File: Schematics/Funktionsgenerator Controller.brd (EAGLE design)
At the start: 58 x 51.3 mm, 35 parts, among them IC1 ATMEGA328PB-AU, IC2 TLE4270-2D, IC3 AD9833BRMZ, IC4 LM318D, IC5 LM318D, X1 22-23-2051, X3 22-23-2031, X4 22-23-2031, X5 22-23-2031, X6 22-23-2031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

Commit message: Added Resistor to limit current for TFT Backlight
Das TFT Display wurde zu heiß, da der Vorwiderstand für die Hintergrundbeleuchtung des TFT lediglich 6Ohm beträgt. Durch einen weiteren Vorwiderstand von 22Ohm konnte die Wärmeentwicklung des Displays erheblich reduziert werden ohne eine merkliche Reduzierung der Helligkeit. Alternativ wäre zu überlegen ob ein Trimmer zur Justierung eingebaut werden sollte
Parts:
- removed C3: EEEFT1V470AR, SamacSys_Parts:EEEFT(C)
- added C15: TAJD476K010R, SamacSys_Parts:CAPPM7344X310N
- added R7: 22, resistor:R0603
- C1, C11, C12, C13, C14, C7, C8: value 100nF -> 100n
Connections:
- new net N$18: P1.LED+, R7.1
- net GND: now also C15.2; no longer C3.2
- net VCC: now also C15.1, R7.2; no longer C3.1, P1.LED+
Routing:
- net VCC: track 178.8 -> 173.3 mm
- net N$18: track 0.00 -> 2.96 mm
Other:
- board text removed: "C:/Users/dem40095/Downloads/404px-sam_and_max_sth.bmp"
- board text removed: "C:/Users/dem40095/Downloads/flat,800x800,075,f.u5.bmp"

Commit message: VCC on encoder connector for external pull-up
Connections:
- net GND: no longer X1.4
- net VCC: now also X1.4
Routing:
- net VCC: track 173.3 -> 186.4 mm
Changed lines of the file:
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@@
 <layer number="14" name="Route14" color="1" fill="6" visible="no" active="no"/>
 <layer number="15" name="Route15" color="4" fill="6" visible="no" active="no"/>
-<layer number="16" name="Bottom" color="1" fill="1" visible="yes" active="yes"/>
+<layer number="16" name="Bottom" color="1" fill="1" visible="no" active="yes"/>
 <layer number="17" name="Pads" color="2" fill="1" visible="yes" active="yes"/>
 <layer number="18" name="Vias" color="2" fill="1" visible="yes" active="yes"/>
@@
 <layer number="20" name="Dimension" color="24" fill="1" visible="yes" active="yes"/>
 <layer number="21" name="tPlace" color="7" fill="1" visible="yes" active="yes"/>
-<layer number="22" name="bPlace" color="7" fill="1" visible="yes" active="yes"/>
+<layer number="22" name="bPlace" color="7" fill="1" visible="no" active="yes"/>
 <layer number="23" name="tOrigins" color="15" fill="1" visible="yes" active="yes"/>
-<layer number="24" name="bOrigins" color="15" fill="1" visible="yes" active="yes"/>
+<layer number="24" name="bOrigins" color="15" fill="1" visible="no" active="yes"/>
 <layer number="25" name="tNames" color="7" fill="1" visible="yes" active="yes"/>
-<layer number="26" name="bNames" color="7" fill="1" visible="yes" active="yes"/>
+<layer number="26" name="bNames" color="7" fill="1" visible="no" active="yes"/>
 <layer number="27" name="tValues" color="7" fill="1" visible="no" active="yes"/>
 <layer number="28" name="bValues" color="7" fill="1" visible="no" active="yes"/>
@@
 <layer number="38" name="bTest" color="7" fill="1" visible="no" active="yes"/>
 <layer number="39" name="tKeepout" color="4" fill="11" visible="yes" active="yes"/>
-<layer number="40" name="bKeepout" color="1" fill="11" visible="yes" active="yes"/>
+<layer number="40" name="bKeepout" color="1" fill="11" visible="no" active="yes"/>
 <layer number="41" name="tRestrict" color="4" fill="10" visible="yes" active="yes"/>
-<layer number="42" name="bRestrict" color="1" fill="10" visible="yes" active="yes"/>
+<layer number="42" name="bRestrict" color="1" fill="10" visible="no" active="yes"/>
 <layer number="43" name="vRestrict" color="2" fill="10" visible="no" active="yes"/>
 <layer number="44" name="Drills" color="7" fill="1" visible="no" active="yes"/>
@@
 <layer number="49" name="Reference" color="7" fill="1" visible="no" active="yes"/>
 <layer number="50" name="dxf" color="7" fill="1" visible="no" active="no"/>
-<layer number="51" name="tDocu" color="7" fill="1" visible="yes" active="yes"/>
-<layer number="52" name="bDocu" color="7" fill="1" visible="yes" active="yes"/>
+<layer number="51" name="tDocu" color="7" fill="1" visible="no" active="yes"/>
+<layer number="52" name="bDocu" color="7" fill="1" visible="no" active="yes"/>
 <layer number="53" name="tGND_GNDA" color="7" fill="9" visible="no" active="no"/>
 <layer number="54" name="bGND_GNDA" color="1" fill="9" visible="no" active="no"/>
@@
 <wire x1="40.64" y1="41.91" x2="40.64" y2="43.6" width="0.3048" layer="16"/>
 <wire x1="40.64" y1="43.6" x2="39.37" y2="44.87" width="0.3048" layer="16"/>
+<contactref element="X1" pad="4"/>
+<wire x1="45.5422" y1="34.4297" x2="46.3169" y2="33.655" width="0.3048" layer="1"/>
+<wire x1="46.3169" y1="33.655" x2="52.07" y2="33.655" width="0.3048" layer="1"/>
+<wire x1="52.07" y1="33.655" x2="52.705" y2="34.29" width="0.3048" layer="1"/>
+<wire x1="50.8" y1="38.1" x2="50.038" y2="38.1" width="0.3048" layer="1"/>
+<wire x1="52.705" y1="34.29" x2="52.705" y2="36.195" width="0.3048" layer="1"/>
+<wire x1="52.705" y1="36.195" x2="50.8" y2="38.1" width="0.3048" layer="1"/>
 </signal>
 <signal name="GND">
@@
 <via x="43.4975" y="12.3825" extent="1-16" drill="0.85"/>
 <via x="20.32" y="37.7825" extent="1-16" drill="0.85"/>
-<contactref element="X1" pad="2"/>
-<contactref element="X1" pad="4"/>
 <wire x1="23.055" y1="37.0775" x2="21.025" y2="37.0775" width="0.3048" layer="1"/>
 <wire x1="21.025" y1="37.0775" x2="20.32" y2="37.7825" width="0.3048" layer="1"/>
@@
 <wire x1="36.1125" y1="36.2775" x2="36.195" y2="36.195" width="0.3048" layer="1"/>
 <contactref element="C15" pad="2"/>
+<contactref element="X1" pad="2"/>
 </signal>
 <signal name="+12V">

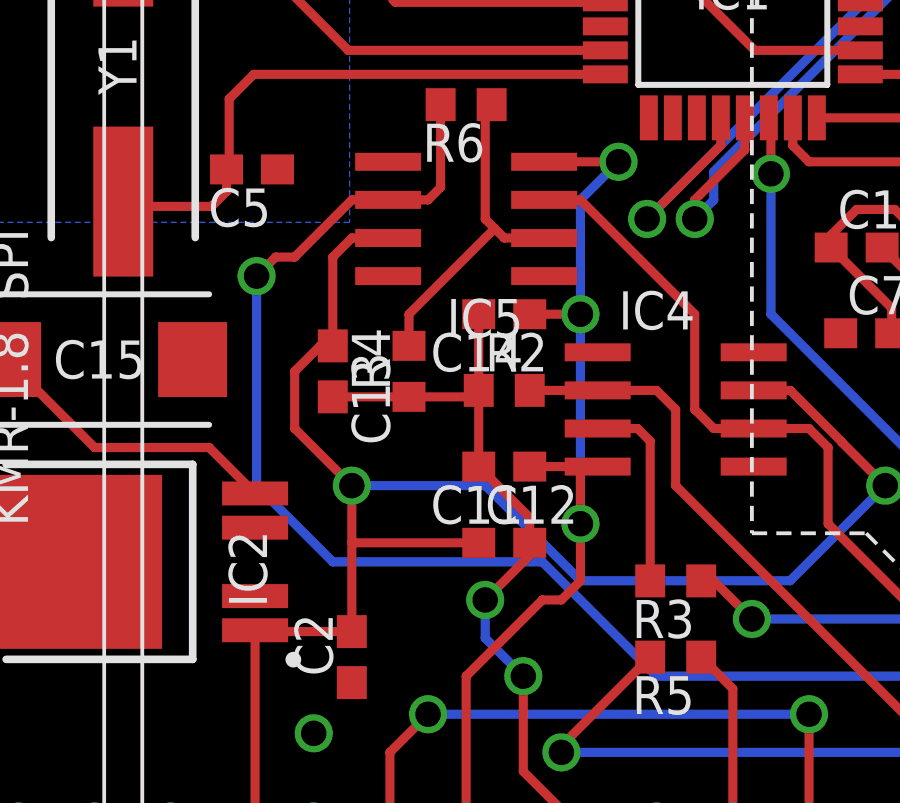
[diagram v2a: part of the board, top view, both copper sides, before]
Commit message: moved labels on, added net names
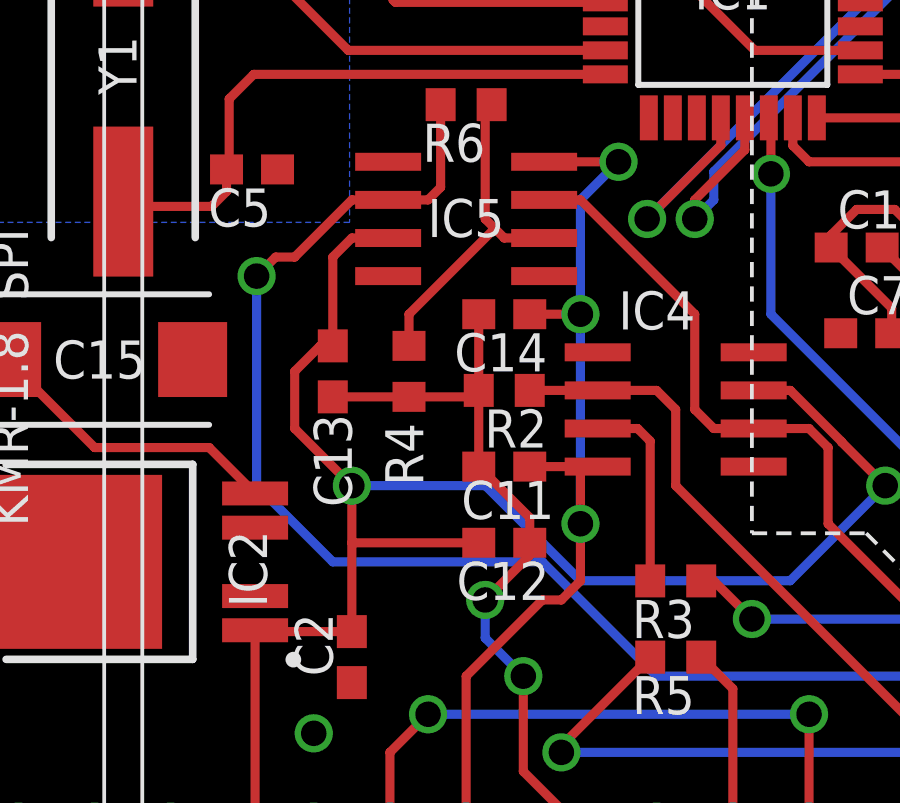
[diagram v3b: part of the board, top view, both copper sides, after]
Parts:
- R2: value 1,3k -> 680
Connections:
- net N$12 renamed ROT_BTN
- net N$13 renamed ROT_B
- net N$14 renamed ROT_A
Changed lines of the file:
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@@
 <setting verticaltext="up"/>
 </settings>
-<grid distance="25" unitdist="mil" unit="mil" style="lines" multiple="1" display="yes" altdistance="5" altunitdist="mil" altunit="mil"/>
+<grid distance="6.25" unitdist="mil" unit="mil" style="lines" multiple="1" display="yes" altdistance="5" altunitdist="mil" altunit="mil"/>
 <layers>
 <layer number="1" name="Top" color="4" fill="1" visible="yes" active="yes"/>
@@
 <element name="IC4" library="linear" library_urn="urn:adsk.eagle:library:262" package="SO08" package3d_urn="urn:adsk.eagle:package:16404/2" value="LM318D" x="25.4" y="21.9075" rot="R270"/>
 <element name="R3" library="resistor" library_urn="urn:adsk.eagle:library:348" package="R0603" package3d_urn="urn:adsk.eagle:package:26057/1" value="1,3k" x="25.4" y="16.1925" rot="R180"/>
-<element name="R2" library="resistor" library_urn="urn:adsk.eagle:library:348" package="R0603" package3d_urn="urn:adsk.eagle:package:26057/1" value="1,3k" x="19.685" y="22.5425"/>
+<element name="R2" library="resistor" library_urn="urn:adsk.eagle:library:348" package="R0603" package3d_urn="urn:adsk.eagle:package:26057/1" value="680" x="19.685" y="22.5425" smashed="yes">
+<attribute name="NAME" x="21.11375" y="21.9075" size="1.27" layer="25" rot="R180"/>
+<attribute name="VALUE" x="19.05" y="20.6375" size="1.27" layer="27"/>
+</element>
 <element name="R5" library="resistor" library_urn="urn:adsk.eagle:library:348" package="R0603" package3d_urn="urn:adsk.eagle:package:26057/1" value="10k" x="25.4" y="13.6525" rot="R180"/>
-<element name="C11" library="resistor" library_urn="urn:adsk.eagle:library:348" package="C0603" package3d_urn="urn:adsk.eagle:package:26138/1" value="100n" x="19.685" y="20.0025" rot="R180"/>
-<element name="C12" library="resistor" library_urn="urn:adsk.eagle:library:348" package="C0603" package3d_urn="urn:adsk.eagle:package:26138/1" value="100n" x="19.685" y="17.4625"/>
+<element name="C11" library="resistor" library_urn="urn:adsk.eagle:library:348" package="C0603" package3d_urn="urn:adsk.eagle:package:26138/1" value="100n" x="19.685" y="20.0025" smashed="yes" rot="R180">
+<attribute name="NAME" x="18.25625" y="18.25625" size="1.27" layer="25"/>
+<attribute name="VALUE" x="20.32" y="21.9075" size="1.27" layer="27" rot="R180"/>
+</element>
+<element name="C12" library="resistor" library_urn="urn:adsk.eagle:library:348" package="C0603" package3d_urn="urn:adsk.eagle:package:26138/1" value="100n" x="19.685" y="17.4625" smashed="yes">
+<attribute name="NAME" x="18.0975" y="15.5575" size="1.27" layer="25"/>
+<attribute name="VALUE" x="19.05" y="15.5575" size="1.27" layer="27"/>
+</element>
 <element name="X7" library="con-molex" library_urn="urn:adsk.eagle:library:165" package="22-23-2021" value="22-23-2021" x="50.4825" y="7.3025" rot="MR180">
 <attribute name="MF" value="MOLEX" x="50.4825" y="7.3025" size="1.778" layer="28" rot="MR180" display="off"/>
@@
 <attribute name="OC_NEWARK" value="30C0862" x="27.305" y="7.3025" size="1.778" layer="28" rot="MR180" display="off"/>
 </element>
-<element name="IC5" library="linear" library_urn="urn:adsk.eagle:library:262" package="SO08" package3d_urn="urn:adsk.eagle:package:16404/2" value="LM318D" x="18.415" y="28.2575" rot="R90"/>
-<element name="C13" library="resistor" library_urn="urn:adsk.eagle:library:348" package="C0603" package3d_urn="urn:adsk.eagle:package:26138/1" value="100n" x="13.97" y="23.1775" rot="R270"/>
-<element name="C14" library="resistor" library_urn="urn:adsk.eagle:library:348" package="C0603" package3d_urn="urn:adsk.eagle:package:26138/1" value="100n" x="19.685" y="25.0825" rot="R180"/>
+<element name="IC5" library="linear" library_urn="urn:adsk.eagle:library:262" package="SO08" package3d_urn="urn:adsk.eagle:package:16404/2" value="LM318D" x="18.415" y="28.2575" smashed="yes" rot="R90">
+<attribute name="NAME" x="19.685" y="28.92425" size="1.27" layer="25" rot="R180"/>
+<attribute name="VALUE" x="20.32" y="32.1945" size="1.27" layer="27" rot="R180"/>
+</element>
+<element name="C13" library="resistor" library_urn="urn:adsk.eagle:library:348" package="C0603" package3d_urn="urn:adsk.eagle:package:26138/1" value="100n" x="13.97" y="23.1775" smashed="yes" rot="R270">
+<attribute name="NAME" x="13.335" y="21.74875" size="1.27" layer="25" rot="R270"/>
+<attribute name="VALUE" x="12.065" y="23.8125" size="1.27" layer="27" rot="R270"/>
+</element>
+<element name="C14" library="resistor" library_urn="urn:adsk.eagle:library:348" package="C0603" package3d_urn="urn:adsk.eagle:package:26138/1" value="100n" x="19.685" y="25.0825" smashed="yes" rot="R180">
+<attribute name="NAME" x="21.11375" y="24.4475" size="1.27" layer="25" rot="R180"/>
+<attribute name="VALUE" x="20.32" y="26.9875" size="1.27" layer="27" rot="R180"/>
+</element>
 <element name="R6" library="resistor" library_urn="urn:adsk.eagle:library:348" package="R0603" package3d_urn="urn:adsk.eagle:package:26057/1" value="10k" x="18.415" y="32.0675" rot="R180"/>
-<element name="R4" library="resistor" library_urn="urn:adsk.eagle:library:348" package="R0603" package3d_urn="urn:adsk.eagle:package:26057/1" value="10k" x="16.51" y="23.1775" rot="R90"/>
+<element name="R4" library="resistor" library_urn="urn:adsk.eagle:library:348" package="R0603" package3d_urn="urn:adsk.eagle:package:26057/1" value="10k" x="16.51" y="23.1775" smashed="yes" rot="R90">
+<attribute name="NAME" x="16.98625" y="19.3675" size="1.27" layer="25" rot="R90"/>
+<attribute name="VALUE" x="18.415" y="22.5425" size="1.27" layer="27" rot="R90"/>
+</element>
 <element name="X1" library="con-molex" library_urn="urn:adsk.eagle:library:165" package="22-23-2051" value="22-23-2051" x="50.038" y="40.64" rot="MR270">
 <attribute name="MF" value="MOLEX" x="50.038" y="40.64" size="1.778" layer="28" rot="MR270" display="off"/>
@@
 <wire x1="26.67" y1="48.0441" x2="26.67" y2="49.53" width="0.3048" layer="16"/>
 </signal>
-<signal name="N$12">
+<signal name="ROT_BTN">
 <contactref element="IC1" pad="31"/>
 <contactref element="X1" pad="1"/>
@@
 <wire x1="45.9105" y1="44.7675" x2="46.863" y2="45.72" width="0.3048" layer="1"/>
 </signal>
-<signal name="N$13">
+<signal name="ROT_B">
 <contactref element="IC1" pad="32"/>
 <contactref element="X1" pad="3"/>
@@
 <wire x1="39.0632" y1="43.2435" x2="36" y2="46.3067" width="0.3048" layer="1"/>
 </signal>
-<signal name="N$14">
+<signal name="ROT_A">
 <contactref element="IC1" pad="1"/>
 <contactref element="X1" pad="5"/>

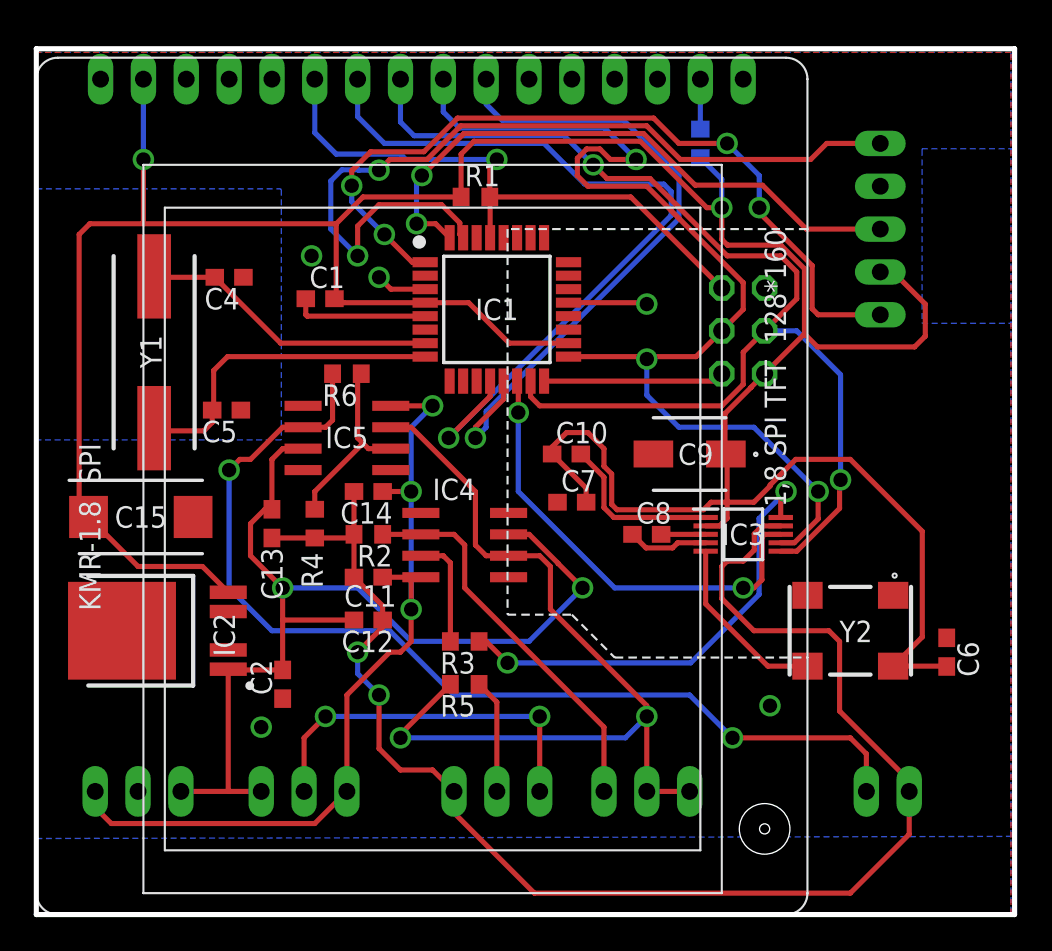
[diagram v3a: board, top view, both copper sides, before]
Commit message: Added trimmer for offset adjustment and some fixes
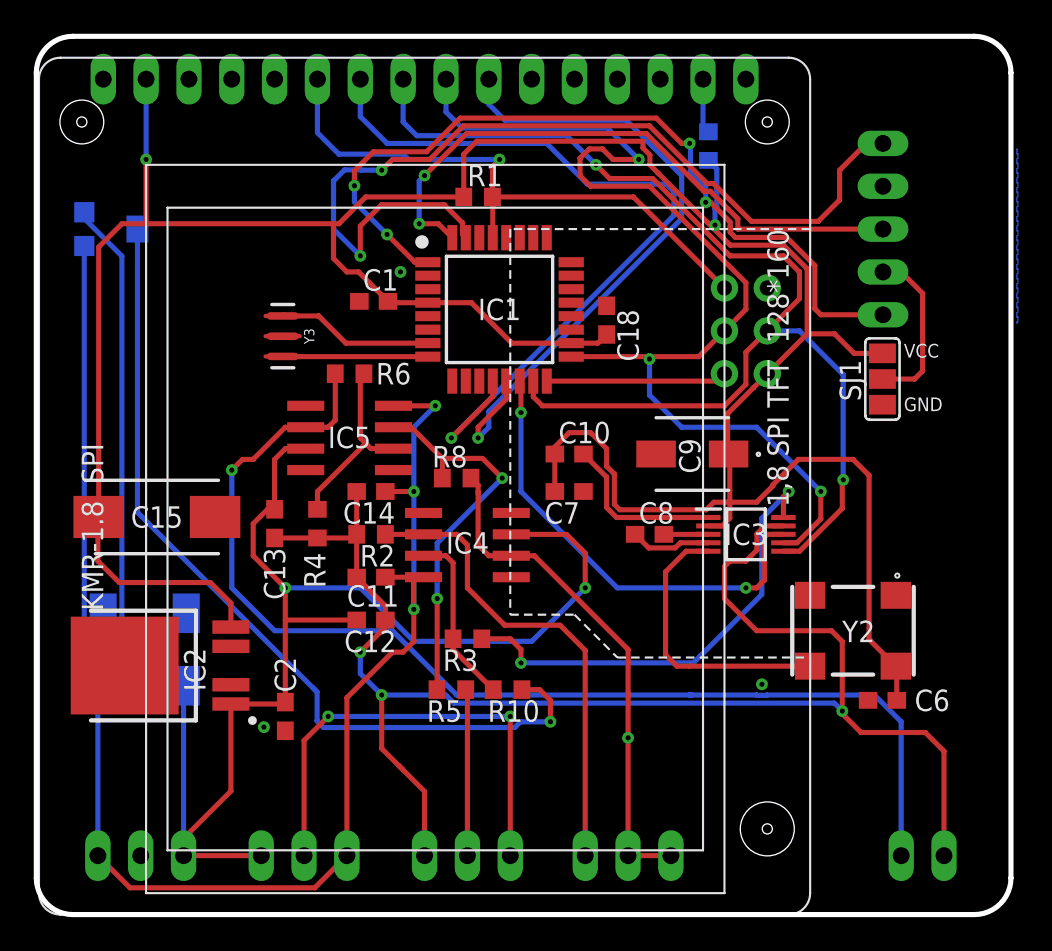
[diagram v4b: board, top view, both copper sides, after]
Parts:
- removed C4, C5: 22p, resistor:C0603
- removed JP1: (no value), pinhead:2X03
- removed Y1: 16MHz, SamacSys_Parts:QCS8.00000F18B23R
- added C16, C17: EEEFK1C100AR, SamacSys_Parts:FKV(B)
- added C18: 100n, resistor:C0603
- added H1: MOUNT-HOLE3.2, holes:3,2
- added ISP1: AVRISP-6, adafruit:AVRISP
- added R10: 1,3k, resistor:R0603
- added R8: 10k, resistor:R0603
- added R9: 1k, user:EVM3ESX50B
- added SJ1: (no value), jumper:SJ_2
- added Y3: 16MHz, SparkFun-Clocks:RESONATOR-SMD-3.2X1.3
- R2: value 680 -> 1,3k
- X3: value 22-23-2031 -> Power Supply
- moved C6 4.76 mm to (50.2, 12.7), turned to 0 degrees
- moved X7 4.33 mm to (52.5, 3.49)
- moved X6 4.19 mm to (25.6, 3.49)
- moved X4 3.97 mm to (35.1, 3.49)
- moved X3 3.81 mm to (6.19, 3.49)
- moved X5 3.81 mm to (15.9, 3.49)
- moved C1 3.18 mm to (20.0, 36.4)
- moved IC2 2.07 mm to (5.24, 14.8)
- moved C2 1.91 mm to (14.8, 11.7)
- moved C15 0.95 mm to (7.15, 23.6)
- moved R5 0.85 mm to (24.6, 13.3)
- moved C7 0.65 mm to (31.6, 25.1), turned to 180 degrees
- moved R7 0.50 mm to (39.8, 45.6)
- moved R3 0.22 mm to (25.6, 16.4)
- moved IC3 0.16 mm to (42.1, 22.5)
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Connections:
- new net N$12: SJ1.2, X1.4
- new net N$13: IC5.3, R5.2, R8.2
- new net N$14: R10.1, R9.2
- net +12V: now also C16.1, R9.3
- net -12V: now also C17.2, R9.1
- net GND: now also C16.2, C17.1, C18.1, ISP1.6, SJ1.3, Y3.2; no longer C4.1, C5.1, JP1.6
- net MISO: now also ISP1.1; no longer JP1.1
- net N$3: now also R10.2
- net N$9: now also R8.1; no longer IC5.3, R5.2
- net RESET: now also ISP1.5; no longer JP1.5
- net SCLK: now also ISP1.3; no longer JP1.3
- net SDATA: now also ISP1.4; no longer JP1.4
- net VCC: now also C18.2, ISP1.2, SJ1.1; no longer JP1.2, X1.4
- net XTAL1: now also Y3.1; no longer C4.2, Y1.1
- net XTAL2: now also Y3.3; no longer C5.2, Y1.2
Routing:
- net N$14: track 0.00 -> 51.1 mm, vias 0 -> 1
- net +12V: track 61.8 -> 108.4 mm
- net -12V: track 50.7 -> 90.6 mm
- net N$13: track 0.00 -> 23.0 mm, vias 0 -> 2
- net N$9: track 52.5 -> 30.4 mm, vias 2 -> 1
- net GND: track 20.7 -> 4.92 mm, vias 5 -> 3
- net XTAL2: track 20.0 -> 8.61 mm
- net N$12: track 0.00 -> 10.1 mm
- net VCC: track 186.4 -> 176.8 mm
- net XTAL1: track 17.7 -> 9.38 mm
- net N$10: track 61.2 -> 68.2 mm, vias 2 -> 1
- net N$1: track 10.7 -> 16.8 mm
- net N$8: track 22.1 -> 27.9 mm
- net N$6: track 23.2 -> 28.4 mm
- net ROT_BTN: track 50.0 -> 54.1 mm
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- removed copper zone on layer 16, net N$15
- removed copper zone on layer 16, net N$17
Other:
- board size 58 x 51.3 mm -> 57.8 x 52.1 mm
- board text added: "+12"
- board text added: "-12"
- board text added: "AGND"
- board text added: "Amplitude"
- board text added: "Btn"
- board text added: "GND"
- board text added: "Offset Adj"
- board text added: "Offset EN"
- board text added: "PSU"
- board text added: "RotA"
- board text added: "RotB"
- board text added: "RotC"
- board text added: "Signal"
- board text added: "Signal Output"
- board text added: "VCC"
- board text added: "VIn"
- board text added: "VOut"
- board text removed: "+12 GND -12 SUPPLY"
- board text removed: "-12 ^ +12 OFFSET"
- board text removed: "AMPLITUDE"
- board text removed: "C:/Users/manni/Downloads/copper_max.bmp"
- board text removed: "FREQUENCY"
- board text removed: "GND FUNC OUTPUT"
- board text removed: "ON/OFF OFFSET"
